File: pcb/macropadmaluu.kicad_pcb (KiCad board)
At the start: 2 copper layers, 86.1 x 47.6 mm, 9 parts, among them SW1 SW_Push, SW2 SW_Push, SW3 SW_Push, SW4 SW_Push, SW5 SW_Push, SW6 SW_Push, U1 XIAO-RP2040-DIP

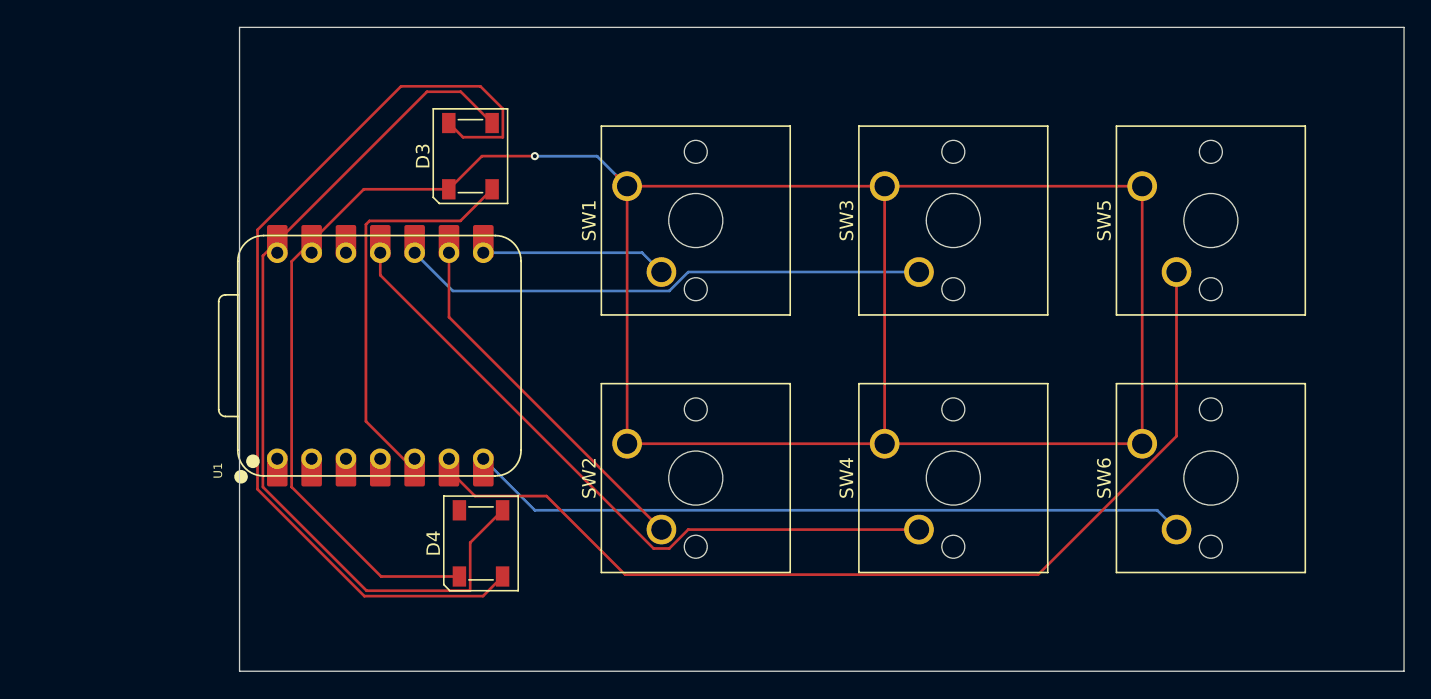
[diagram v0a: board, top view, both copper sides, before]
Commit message: Add Gerber and drill files for macropadmaluu project
- Created non-plated through-hole (NPTH) drill file: macropadmaluu-NPTH.drl
- Created plated through-hole (PTH) drill file: macropadmaluu-PTH.drl
- Added job file for Gerber generation: macropadmaluu-job.gbrjob
- All files generated using KiCad version 9.0.6 with appropriate specifications and attributes.
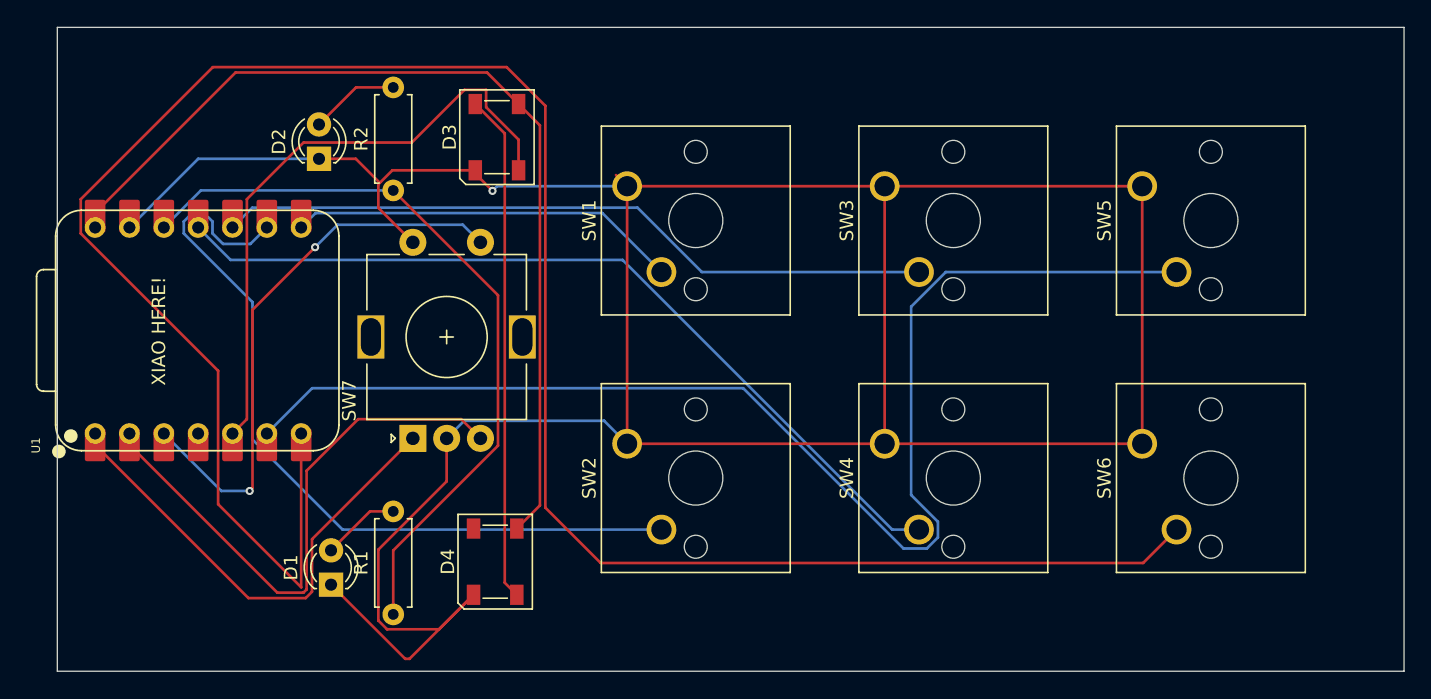
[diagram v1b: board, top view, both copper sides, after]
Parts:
- added D1: LED, LED_THT:LED_D3.0mm, F.Cu at (142.1, 115.0)
- added D2: LED, LED_THT:LED_D3.0mm, F.Cu at (141.2, 83.5)
- added R1: 680Ω, Resistor_THT:R_Axial_DIN0207_L6.3mm_D2.5mm_P7.62mm_Horizontal, F.Cu at (146.7, 117.2)
- added R2: 680Ω, Resistor_THT:R_Axial_DIN0207_L6.3mm_D2.5mm_P7.62mm_Horizontal, F.Cu at (146.7, 85.9)
- added SW7: RotaryEncoder_Switch, Rotary_Encoder:RotaryEncoder_Alps_EC11E-Switch_Vertical_H20mm, F.Cu at (148.1, 104.2)
- moved U1 13.6 mm to (132.3, 96.2)
- moved D3 2.41 mm to (154.4, 81.9)
- moved D4 1.71 mm to (154.2, 113.3)
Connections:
- U1 pad 1: unconnected-(U1-GPIO26/ADC0/A0-Pad1) -> Net-(U1-GPIO26/ADC0/A0)
- U1 pad 12: unconnected-(U1-3V3-Pad12) -> Net-(U1-3V3)
- U1 pad 2: unconnected-(U1-GPIO27/ADC1/A1-Pad2) -> Net-(U1-GPIO27/ADC1/A1)
- U1 pad 3: unconnected-(U1-GPIO28/ADC2/A2-Pad3) -> Net-(U1-GPIO28/ADC2/A2)
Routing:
- net Net-(U1-GPIO0/TX): track 53.4 -> 165.6 mm
- net Net-(U1-3V3): track 0.00 -> 55.9 mm
- net Net-(U1-GPIO27/ADC1/A1): track 0.00 -> 42.4 mm
- net Net-(U1-GPIO28/ADC2/A2): track 0.00 -> 41.6 mm, vias 0 -> 2
- net GND: track 196.1 -> 234.4 mm
- net Net-(U1-GPIO26/ADC0/A0): track 0.00 -> 36.2 mm
- net Net-(D3-DOUT): track 71.1 -> 37.6 mm
- net Net-(U1-GPIO2/SCK): track 27.8 -> 59.6 mm
- net Net-(U1-GPIO7/SCL): track 73.4 -> 94.9 mm
- net Net-(D3-DIN): track 30.1 -> 45.8 mm
- net Net-(U1-GPIO1/RX): track 13.8 -> 28.9 mm
- net Net-(U1-GPIO4/MISO): track 39.1 -> 53.4 mm
- net Net-(U1-GPIO3/MOSI): track 50.5 -> 62.6 mm
- net Net-(D2-A): track 0.00 -> 6.62 mm
- net Net-(D1-A): track 0.00 -> 5.79 mm
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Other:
- board size 86.1 x 47.6 mm -> 99.6 x 47.6 mm
- board text added: "XIAO HERE!"
- board text removed: "XIAO HERE!!"
